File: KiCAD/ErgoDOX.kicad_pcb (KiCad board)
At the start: 2 copper layers, 182.8 x 158.9 mm, 114 parts, among them J1 USB, J2 3.5mm, J3 JMP, J4 JMP, J5 JMP, J6 JMP, J7 USB, SW1 SWITCH_PUSH, SW10 SWITCH_PUSH, SW11 SWITCH_PUSH, SW12 SWITCH_PUSH, SW13 SWITCH_PUSH, SW14 SWITCH_PUSH, SW15 SWITCH_PUSH, SW16 SWITCH_PUSH, SW17 SWITCH_PUSH, SW18 SWITCH_PUSH, SW19 SWITCH_PUSH, SW2 SWITCH_PUSH, SW20 SWITCH_PUSH, SW21 SWITCH_PUSH, SW22 SWITCH_PUSH, SW23 SWITCH_PUSH, SW24 SWITCH_PUSH, SW25 SWITCH_PUSH, SW26 SWITCH_PUSH, SW27 SWITCH_PUSH, SW28 SWITCH_PUSH, SW29 SWITCH_PUSH, SW3 SWITCH_PUSH, SW30 SWITCH_PUSH, SW31 SWITCH_PUSH, SW32 SWITCH_PUSH, SW33 SWITCH_PUSH, SW34 SWITCH_PUSH, SW35 SWITCH_PUSH, SW36 SWITCH_PUSH, SW37 SWITCH_PUSH, SW38 SWITCH_PUSH, SW39 SWITCH_PUSH, SW4 SWITCH_PUSH, SW40 SWITCH_PUSH, SW41 SWITCH_PUSH, SW42 SWITCH_PUSH, SW43 SWITCH_PUSH, SW44 SWITCH_PUSH, SW45 SWITCH_PUSH, SW46 SWITCH_PUSH, SW5 SWITCH_PUSH, SW6 SWITCH_PUSH, SW7 SWITCH_PUSH, SW8 SWITCH_PUSH, SW9 SWITCH_PUSH, U1 ProMicro

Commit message: added in switch LED
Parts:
- added D41: LED, BishopKicadConsolidated:CHERRY_MX_LED, F.Cu at (72.4, 65.1)
- added D42: LED, BishopKicadConsolidated:CHERRY_MX_LED, F.Cu at (91.4, 65.1)
- added D43: LED, BishopKicadConsolidated:CHERRY_MX_LED, F.Cu at (110.5, 63.9)
- added D44: LED, BishopKicadConsolidated:CHERRY_MX_LED, F.Cu at (129.5, 62.2)
- added D45: LED, BishopKicadConsolidated:CHERRY_MX_LED, F.Cu at (148.7, 63.8)
- added D46: LED, BishopKicadConsolidated:CHERRY_MX_LED, F.Cu at (167.6, 67.1)
- added D47: LED, BishopKicadConsolidated:CHERRY_MX_LED, F.Cu at (72.4, 88.9)
- added D48: LED, BishopKicadConsolidated:CHERRY_MX_LED, F.Cu at (91.4, 84.2)
- added D49: LED, BishopKicadConsolidated:CHERRY_MX_LED, F.Cu at (110.5, 82.9)
- added D50: LED, BishopKicadConsolidated:CHERRY_MX_LED, F.Cu at (129.5, 81.3)
- added D51: LED, BishopKicadConsolidated:CHERRY_MX_LED, F.Cu at (148.6, 82.9)
- added D52: LED, BishopKicadConsolidated:CHERRY_MX_LED, F.Cu at (167.6, 86.1)
- added D53: LED, BishopKicadConsolidated:CHERRY_MX_LED, F.Cu at (91.4, 103.2)
- added D54: LED, BishopKicadConsolidated:CHERRY_MX_LED, F.Cu at (110.5, 101.9)
- added D55: LED, BishopKicadConsolidated:CHERRY_MX_LED, F.Cu at (129.5, 100.3)
- added D56: LED, BishopKicadConsolidated:CHERRY_MX_LED, F.Cu at (148.6, 102.0)
- added D57: LED, BishopKicadConsolidated:CHERRY_MX_LED, F.Cu at (167.6, 105.1)
- added D58: LED, BishopKicadConsolidated:CHERRY_MX_LED, F.Cu at (72.4, 117.5)
- added D59: LED, BishopKicadConsolidated:CHERRY_MX_LED, F.Cu at (91.4, 122.2)
- added D60: LED, BishopKicadConsolidated:CHERRY_MX_LED, F.Cu at (110.5, 121.0)
- added D61: LED, BishopKicadConsolidated:CHERRY_MX_LED, F.Cu at (129.5, 119.4)
- added D62: LED, BishopKicadConsolidated:CHERRY_MX_LED, F.Cu at (148.6, 121.0)
- added D63: LED, BishopKicadConsolidated:CHERRY_MX_LED, F.Cu at (167.6, 124.2)
- added D64: LED, BishopKicadConsolidated:CHERRY_MX_LED, F.Cu at (34.7, 143.3)
- added D65: LED, BishopKicadConsolidated:CHERRY_MX_LED, F.Cu at (52.0, 135.2)
- added D66: LED, BishopKicadConsolidated:CHERRY_MX_LED, F.Cu at (42.7, 160.5)
- added D67: LED, BishopKicadConsolidated:CHERRY_MX_LED, F.Cu at (50.8, 177.8)
- added D68: LED, BishopKicadConsolidated:CHERRY_MX_LED, F.Cu at (64.0, 161.1)
- added D69: LED, BishopKicadConsolidated:CHERRY_MX_LED, F.Cu at (110.5, 140.0)
- added D70: LED, BishopKicadConsolidated:CHERRY_MX_LED, F.Cu at (81.3, 153.1)
- added D71: LED, BishopKicadConsolidated:CHERRY_MX_LED, F.Cu at (129.5, 138.4)
- added D72: LED, BishopKicadConsolidated:CHERRY_MX_LED, F.Cu at (148.6, 140.1)
- added D73: LED, BishopKicadConsolidated:CHERRY_MX_LED, F.Cu at (167.6, 143.2)
- added D74: LED, BishopKicadConsolidated:CHERRY_MX_LED, F.Cu at (186.7, 143.2)
- added D75, D76, D77, D78, D79, D80: LED, BishopKicadConsolidated:CHERRY_MX_LED, F.Cu at (127.6, 198.4)
- added J8: Conn_01x05, Pin_Headers:Pin_Header_Straight_1x05_Pitch2.54mm, F.Cu at (132.6, 39.5)
- added Q1: BSS138, TO_SOT_Packages_SMD:SOT-23, F.Cu at (154.7, 38.2)
- added R10, R11, R12, R13, R14, R15, R16, R17, R18, R21, R22, R23, R24, R25, R26, R27, R28, R29, R30, R31, R32, R33, R34, R35, R36, R37, R38, R39, R4, R40, R41, R42, R43, R44, R5, R6, R7, R8, R9: 470, SMD_Packages:SMD-1206_Pol, F.Cu at (114.5, 199.5)
- added R19: 100, SMD_Packages:SMD-1206_Pol, F.Cu at (146.9, 43.6)
- added R20: 100, SMD_Packages:SMD-1206_Pol, F.Cu at (148.7, 45.3)
- added R3: 470, SMD_Packages:SMD-1206_Pol, F.Cu at (125.0, 176.1)
- moved JP1 169.3 mm to (114.5, 199.5), turned to 0 degrees
- moved JP2 165.3 mm to (114.5, 199.5), turned to 0 degrees
- moved RC1 93.5 mm to (33.0, 61.1)
- moved LED_C1 50.2 mm to (22.2, 116.1)
- moved RB1 35.5 mm to (146.0, 8.02)
- moved LED_B1 34.8 mm to (38.9, 79.3)
- moved RA1 34.8 mm to (149.9, 10.6)
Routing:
- net GND: track 2.27 -> 38.2 mm, vias 3 -> 4
- net /D-: track 0.00 -> 24.0 mm
- net VCC: track 101.7 -> 122.0 mm, vias 3 -> 4
- net /ID: track 0.00 -> 14.3 mm, vias 0 -> 1
- net /D+: track 0.00 -> 6.86 mm
- net /COL1: track 168.5 -> 170.4 mm
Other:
- board text added: "GND ID D+ D- VCC"
- board text added: "VCC D- D+ ID GND"

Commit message: led's placed
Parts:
- removed JP1, JP2: JUMPER, BishopKicadConsolidated:SOLDER_JUMPER_2
- removed LED_B1: LEDb, footprints:CHERRY_MX_LED
- removed LED_C1: LEDc, footprints:CHERRY_MX_LED
- removed RA1: LEDa, footprints:RESISTOR
- removed RB1: LEDb, footprints:RESISTOR
- removed RC1: LEDc, footprints:RESISTOR
- R10, R11, R12, R13, R14, R15, R16, R17, R18, R21, R22, R23, R24, R25, R26, R27, R28, R29, R3, R30, R31, R32, R33, R34, R35, R36, R37, R38, R39, R4, R40, R41, R42, R43, R44, R5, R6, R7, R8, R9: moved to B.Cu
- moved R8 146.1 mm to (176.7, 67.4), turned to 90 degrees
- moved R7 142.4 mm to (157.6, 63.8), turned to 90 degrees
- moved R6 139.6 mm to (138.6, 62.0), turned to 90 degrees
- moved R5 135.8 mm to (119.5, 63.8), turned to 90 degrees
- moved R4 135.3 mm to (100.5, 65.0), turned to 90 degrees
- moved R14 129.6 mm to (176.7, 85.8), turned to 90 degrees
- moved R9 126.8 mm to (72.5, 79.9), turned to 180 degrees
- moved R13 124.4 mm to (157.6, 82.9), turned to 90 degrees
- moved R12 120.9 mm to (138.6, 81.1), turned to 90 degrees
- moved R3 119.4 mm to (81.4, 65.0)
- moved R11 116.8 mm to (119.5, 82.9), turned to 90 degrees
- moved R10 116.3 mm to (100.5, 84.0), turned to 90 degrees
- moved R21 113.3 mm to (176.7, 104.9), turned to 90 degrees
- moved R18 106.7 mm to (157.6, 101.9), turned to 90 degrees
- moved R17 102.3 mm to (138.6, 100.1), turned to 90 degrees
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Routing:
- net /ROW1: track 234.2 -> 238.4 mm
- net /ROW4: track 176.3 -> 179.2 mm
- net /ROW3: track 151.8 -> 153.2 mm

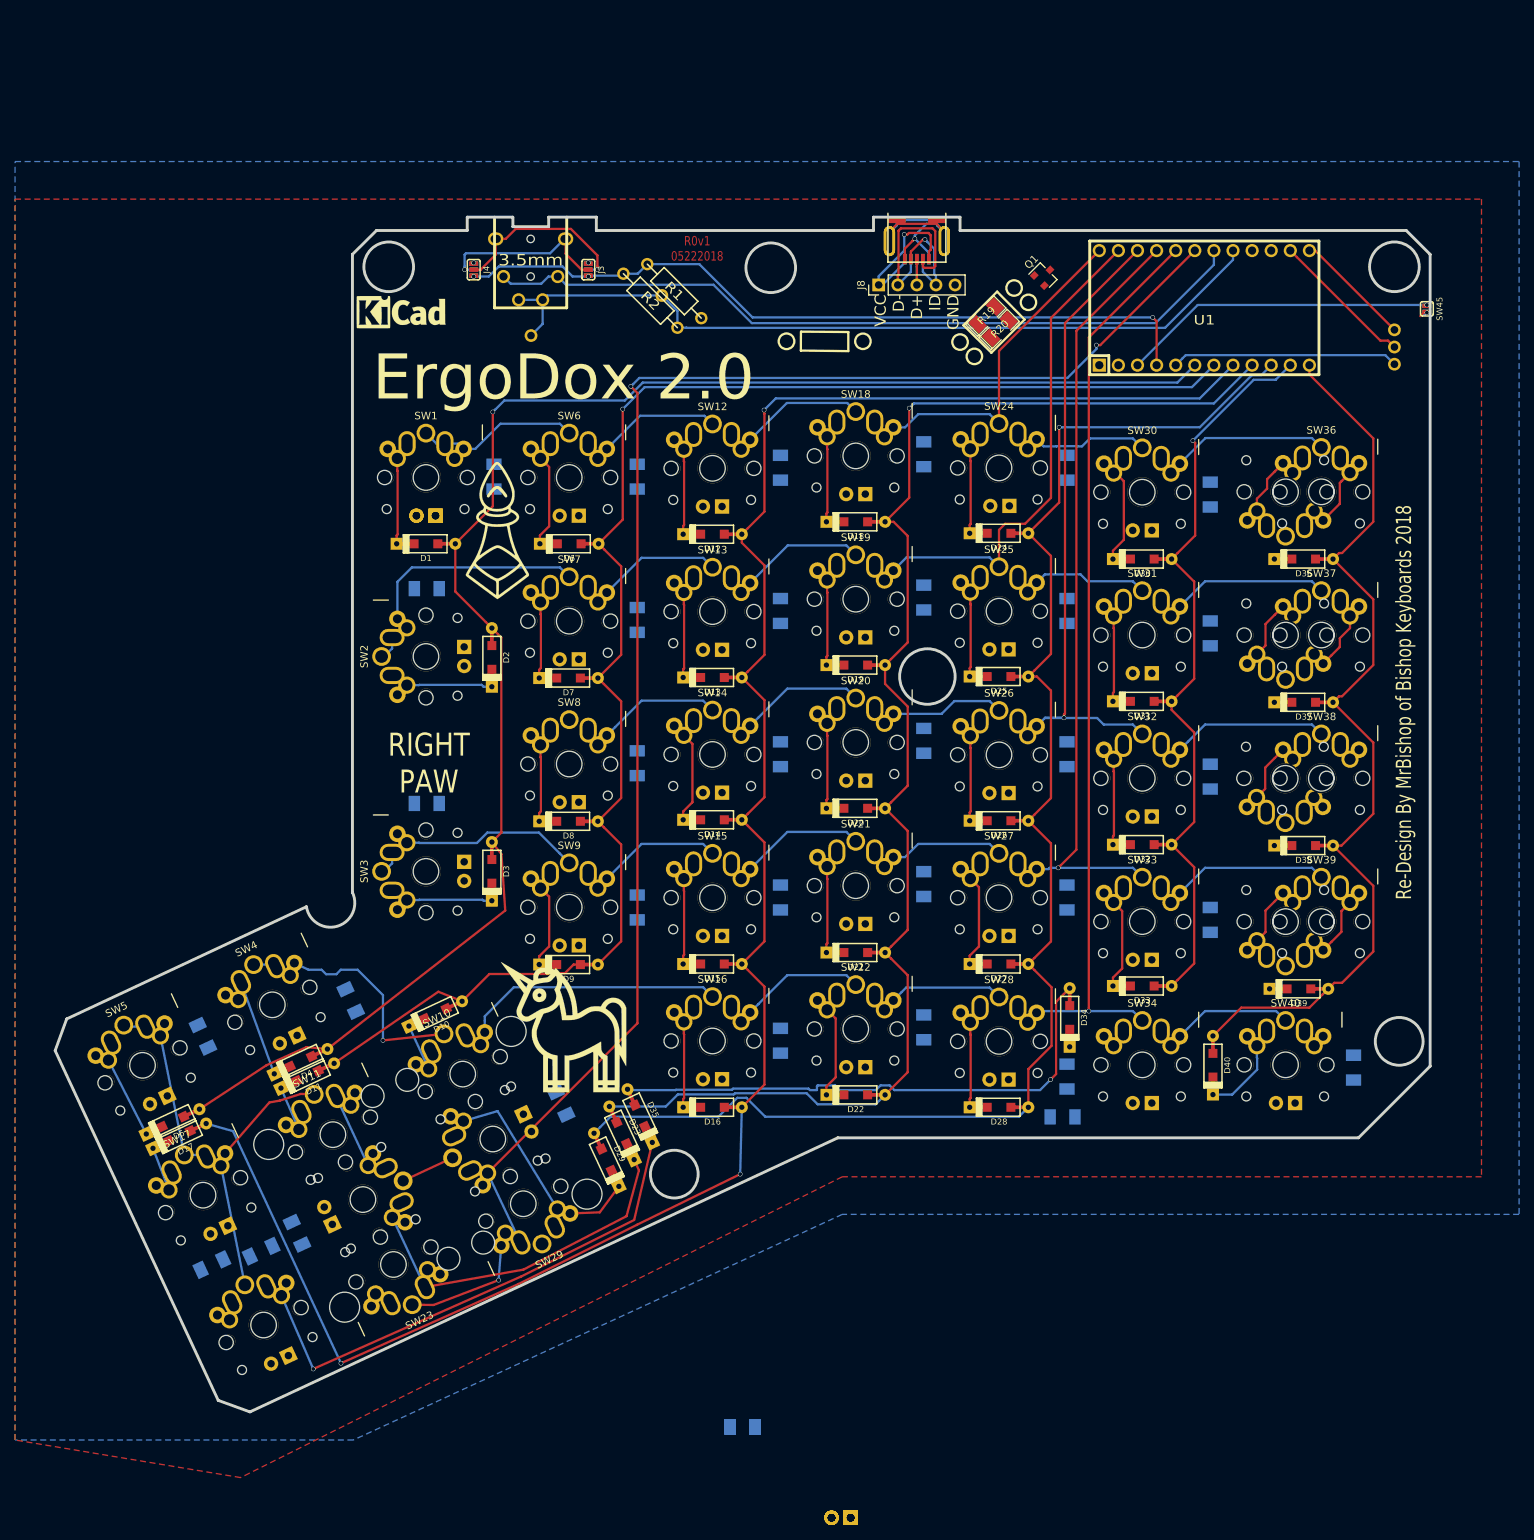
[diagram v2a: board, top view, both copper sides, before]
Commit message: led circuit and placement
finisehd placing led components and traces
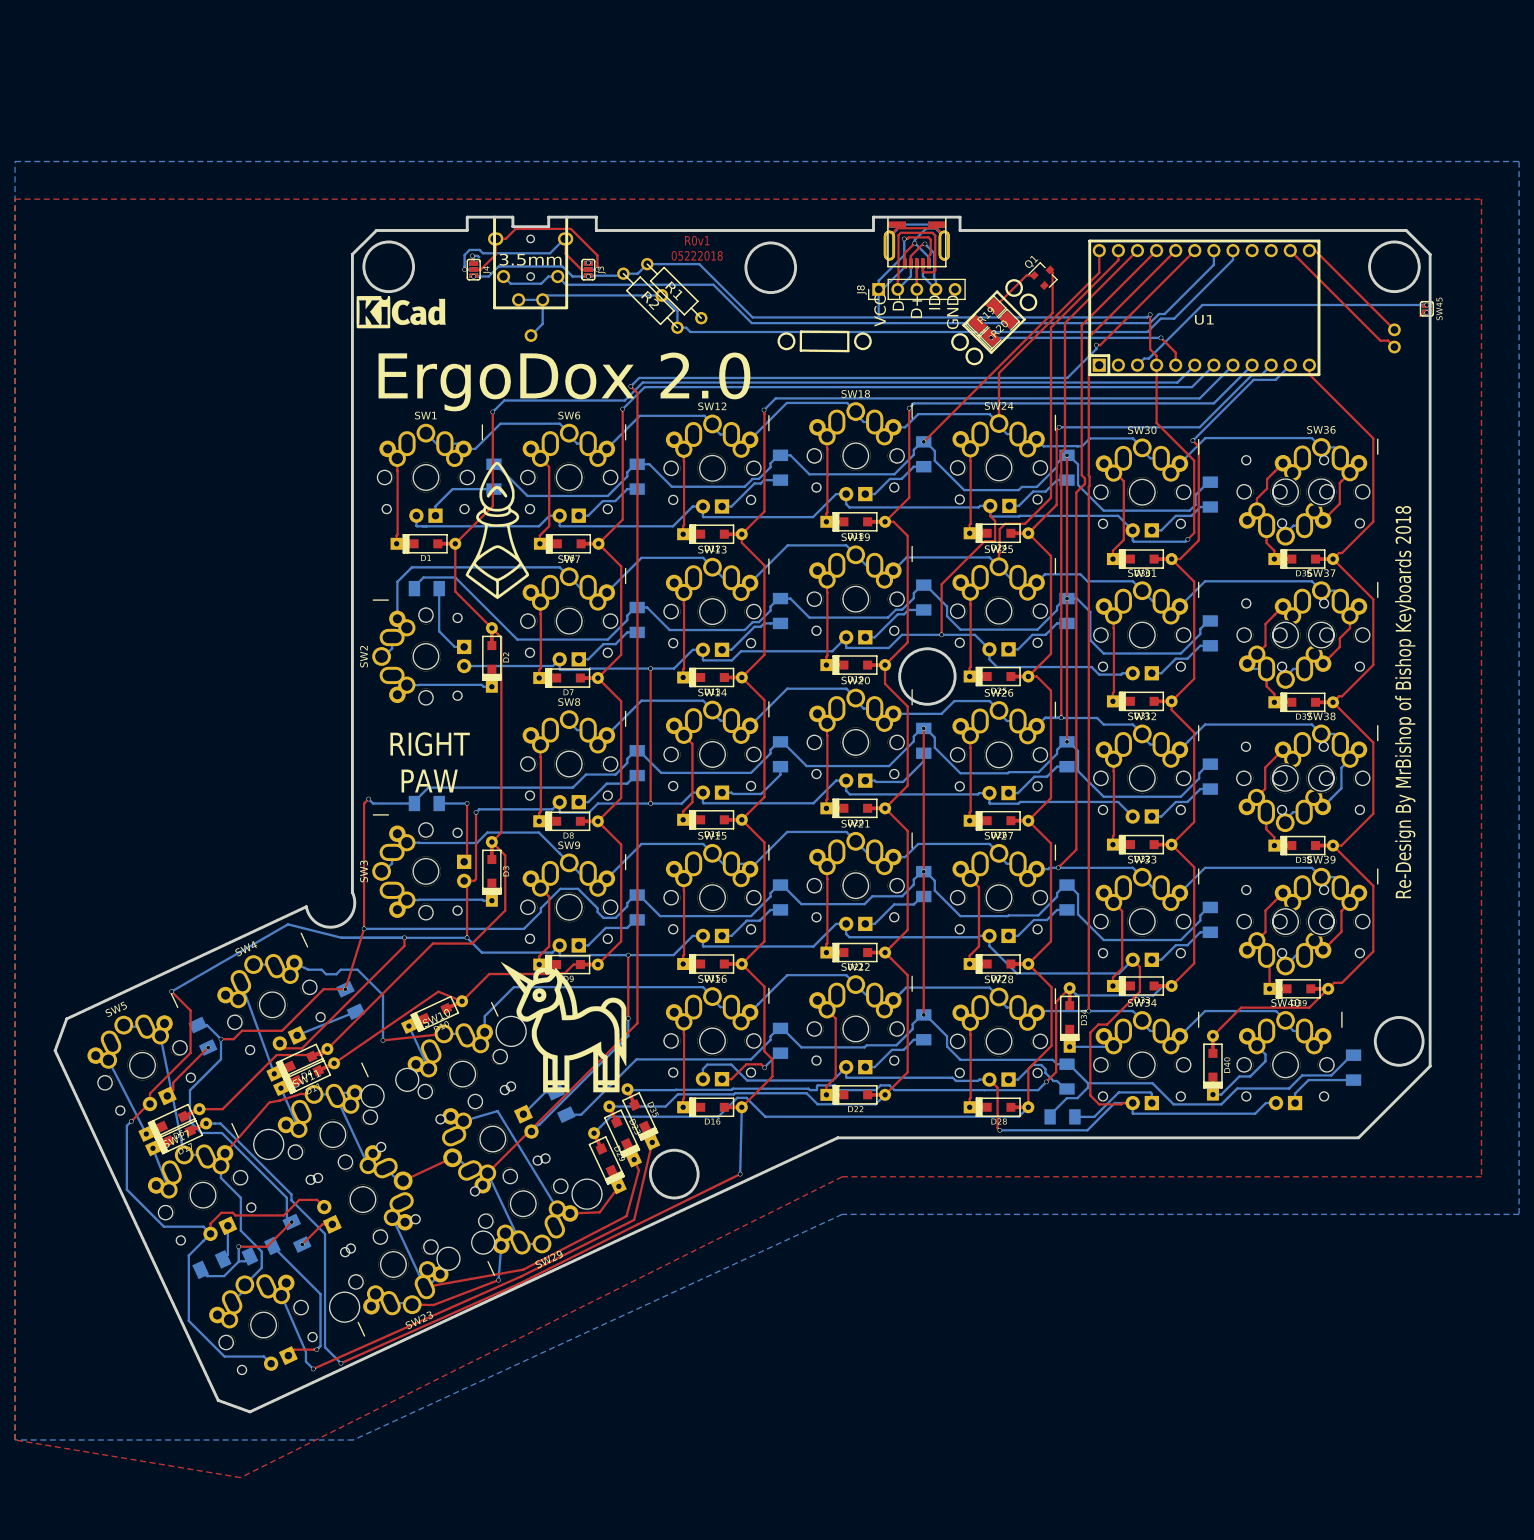
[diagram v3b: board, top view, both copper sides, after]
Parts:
- removed D75, D76, D77, D78, D79, D80: LED, BishopKicadConsolidated:CHERRY_MX_LED
- removed LED_A1: LEDa, footprints:CHERRY_MX_LED
- removed R39, R40, R41, R42, R43, R44: 470, SMD_Packages:SMD-1206_Pol
- removed W5: TEST_1P, BishopKicadConsolidated:PIN_1
- moved J1 0.60 mm to (137.7, 36.7)
- moved J7 0.60 mm to (137.7, 36.7)
- moved J8 0.60 mm to (132.6, 40.1)
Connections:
- U1 pad 5: Net-(U1-Pad5) -> /backlight
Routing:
- net Net-(Q1-Pad3): track 0.00 -> 856.4 mm, vias 0 -> 13
- net VCC: track 122.0 -> 931.2 mm, vias 4 -> 16
- net /ROW3: track 153.2 -> 213.9 mm
- net /ROW5: track 144.2 -> 197.2 mm
- net /ROW2: track 210.5 -> 263.2 mm
- net /ROW4: track 179.2 -> 231.2 mm
- net /ROW0: track 302.4 -> 349.6 mm
- net /ROW1: track 238.4 -> 283.3 mm
- net Net-(U1-Pad5): track 30.1 -> 0.00 mm
- net /backlight: track 0.00 -> 29.6 mm, vias 0 -> 2
- net Net-(D67-Pad2): track 0.00 -> 20.8 mm, vias 0 -> 1
- net /COL1: track 170.4 -> 185.8 mm
- net Net-(D37-Pad1): track 7.78 -> 21.6 mm
- net Net-(D38-Pad1): track 7.80 -> 21.3 mm
- net Net-(D36-Pad1): track 7.78 -> 21.3 mm
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
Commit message: updated picture
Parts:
- added G***: LOGO, Silks:USFlag2, B.Cu at (72.5, 46.5)
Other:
- board text added: "Designed with Freedom"
- board text added: "Name is work in progress"
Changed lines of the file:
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@@
 (kicad_pcb (version 4) (host pcbnew 4.0.7)
   (general
-    (links 678)
-    (no_connects 3)
+    (links 0)
+    (no_connects 1)
     (area 22.890479 30.289499 206.108301 189.542421)
     (thickness 1.6002)
-    (drawings 52)
+    (drawings 57)
     (tracks 1955)
     (zones 0)
-    (modules 177)
+    (modules 178)
     (nets 103)
   )
@@
     (34 B.Paste user)
     (35 F.Paste user)
-    (36 B.SilkS user hide)
+    (36 B.SilkS user)
     (37 F.SilkS user)
     (38 B.Mask user)
@@
     )
   )
+  (module Silks:USFlag2 (layer Back)
+    (at 72.501066 46.537557 180)
+    (fp_text reference G*** (at 0 0 180) (layer B.SilkS) hide
+      (effects (font (thickness 0.3)) (justify mirror))
+    )
+    (fp_text value LOGO (at 0.75 0 180) (layer B.SilkS) hide
+      (effects (font (thickness 0.3)) (justify mirror))
+    )
+    (fp_poly (pts (xy 9.21766 -5.08762) (xy -9.21512 -5.08762) (xy -9.21512 -4.33578) (xy 9.21766 -4.33578)
+      (xy 9.21766 -5.08762)) (layer B.SilkS) (width 0.01))
+    (fp_poly (pts (xy 9.21766 -3.5179) (xy -9.21512 -3.5179) (xy -9.21512 -2.76606) (xy 9.21766 -2.76606)
+      (xy 9.21766 -3.5179)) (layer B.SilkS) (width 0.01))
+    (fp_poly (pts (xy 9.217676 -1.94818) (xy -9.215137 -1.94818) (xy -9.214494 -1.571625) (xy -9.21385 -1.19507)
+      (xy 9.21639 -1.19507) (xy 9.217676 -1.94818)) (layer B.SilkS) (width 0.01))
+    (fp_poly (pts (xy -2.986405 5.086764) (xy -2.796717 5.086714) (xy -2.605685 5.086664) (xy -2.41343 5.086614)
+      (xy -2.220072 5.086565) (xy -2.025731 5.086517) (xy -1.830529 5.086468) (xy -1.634584 5.086421)
+      (xy -1.438018 5.086373) (xy -1.240951 5.086326) (xy -1.043502 5.08628) (xy -0.845794 5.086234)
+      (xy -0.647944 5.086189) (xy -0.450076 5.086145) (xy -0.252307 5.086101) (xy -0.054759 5.086057)
+      (xy 0.142448 5.086015) (xy 0.339193 5.085973) (xy 0.535357 5.085931) (xy 0.730818 5.085891)
+      (xy 0.925458 5.085851) (xy 1.119154 5.085812) (xy 1.311788 5.085773) (xy 1.503238 5.085736)
+      (xy 1.693385 5.085699) (xy 1.882107 5.085663) (xy 2.069286 5.085628) (xy 2.254799 5.085594)
+      (xy 2.438528 5.085561) (xy 2.620351 5.085529) (xy 2.800149 5.085498) (xy 2.977801 5.085467)
+      (xy 3.153187 5.085438) (xy 3.326186 5.08541) (xy 3.496678 5.085383) (xy 3.664543 5.085357)
+      (xy 3.82966 5.085332) (xy 3.991909 5.085308) (xy 4.151171 5.085285) (xy 4.307323 5.085263)
+      (xy 4.460247 5.085243) (xy 4.609822 5.085223) (xy 4.755927 5.085205) (xy 4.898442 5.085189)
+      (xy 5.037247 5.085173) (xy 5.172222 5.085159) (xy 5.303245 5.085146) (xy 5.430198 5.085134)
+      (xy 5.552959 5.085124) (xy 5.671408 5.085115) (xy 5.785426 5.085108) (xy 5.89489 5.085102)
+      (xy 5.999682 5.085097) (xy 6.099681 5.085094) (xy 6.194767 5.085092) (xy 6.229985 5.085092)
+      (xy 9.21766 5.08508) (xy 9.21766 4.33324) (xy -0.8128 4.33324) (xy -0.8128 3.51536)
+      (xy 9.21766 3.51536) (xy 9.21766 2.76352) (xy -0.8128 2.76352) (xy -0.8128 1.94564)
+      (xy 9.217676 1.94564) (xy 9.21639 1.19253) (xy -0.812801 1.19253) (xy -0.812801 0.784225)
+      (xy -0.8128 0.37592) (xy 4.203065 0.375921) (xy 9.21893 0.375921) (xy 9.218278 -0.001269)
+      (xy 9.217626 -0.37846) (xy -9.21512 -0.37846) (xy -9.21512 5.088424) (xy -2.986405 5.086764)) (layer B.SilkS) (width 0.01))
+  )
+  (gr_line (start 199.302735 49.514122) (end 201.088674 49.514122) (layer B.SilkS) (width 0.3048))
+  (gr_line (start 199.302735 43.560992) (end 199.302735 49.514122) (layer B.SilkS) (width 0.3048))
+  (gr_line (start 201.088674 43.560992) (end 199.302735 43.560992) (layer B.SilkS) (width 0.3048))
+  (gr_text "Name is work in progress" (at 92.146395 56.657878) (layer F.SilkS)
+    (effects (font (size 2.032 1.524) (thickness 0.3048)))
+  )
+  (gr_text "Designed with\nFreedom" (at 72.501066 54.871939) (layer B.SilkS)
+    (effects (font (size 2.032 1.524) (thickness 0.3048)) (justify mirror))
+  )
   (gr_line (start 122.2375 48.2219) (end 122.2502 45.7073) (layer F.SilkS) (width 0.3048))
